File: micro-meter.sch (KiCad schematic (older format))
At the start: 110 parts, among them U1 XC6206P332MR, U2 STM32F411CEU6

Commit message: Fix testpoints
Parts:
- removed TP?: TP_3V3, symbol Connector:TestPoint_2Pole
- removed TP?: TP_I2S, symbol Connector:TestPoint_2Pole
- removed TP?: TP_AIN1, symbol Connector:TestPoint_2Pole
- added R?: 390, symbol Device:R
- added TP?: TP_AIN1, symbol Connector:TestPoint
- added TP? (x3): TP_GND, symbol Connector:TestPoint
- added TP?: TP_DIN, symbol Connector:TestPoint
- added TP?: TP_3V3, symbol Connector:TestPoint
- TP?: symbol Connector:TestPoint_2Pole -> Connector:TestPoint
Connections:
- net +3V3: now also TP?.1
- net AIN1: now also TP?.1
- net GND: now also TP?.1, TP?.1, TP?.1; no longer TP?.2
- net USART1_TX: now also R?.2; no longer U2.30 (PA9)
- net at D?.4 (DIN), R?.1: now also TP?.1
- new net: R?.1, U2.30 (PA9)
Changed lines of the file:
@@
 Comment4 ""
 $EndDescr
-Text GLabel 2300 3250 2    50   Output ~ 0
+Text GLabel 2600 3250 2    50   Output ~ 0
 USART1_TX
 Text GLabel 2300 3350 2    50   Input ~ 0
@@
 	9400 1400 9500 1400
 $Comp
-L Connector:TestPoint_2Pole TP?
+L Connector:TestPoint TP?
 U 1 1 5FAA848A
-P 6850 1800
-F 0 "TP?" V 6800 1650 50  0000 C CNN
-F 1 "TP_AIN0" V 6900 1600 50  0000 C CNN
-F 2 "" H 6850 1800 50  0001 C CNN
-F 3 "~" H 6850 1800 50  0001 C CNN
-	1    6850 1800
-	0    -1   1    0
-$EndComp
-$Comp
-L power:GND #PWR?
-U 1 1 5FAAECA1
-P 6850 2000
-F 0 "#PWR?" H 6850 1750 50  0001 C CNN
-F 1 "GND" H 6855 1827 50  0000 C CNN
-F 2 "" H 6850 2000 50  0001 C CNN
-F 3 "" H 6850 2000 50  0001 C CNN
-	1    6850 2000
-	1    0    0    -1
+P 6850 1600
+F 0 "TP?" H 7000 1750 50  0000 C CNN
+F 1 "TP_AIN0" H 7050 1850 50  0000 C CNN
+F 2 "" H 6850 1600 50  0001 C CNN
+F 3 "~" H 6850 1600 50  0001 C CNN
+	1    6850 1600
+	1    0    0    1
 $EndComp
 $Comp
@@
 Text GLabel 1000 3250 0    50   Output ~ 0
 I2S5_SD
-$Comp
-L Connector:TestPoint_2Pole TP?
-U 1 1 5FAE18DF
-P 3350 5050
-F 0 "TP?" V 3300 5250 50  0000 R CNN
-F 1 "TP_I2S" V 3400 5350 50  0000 R CNN
-F 2 "" H 3350 5050 50  0001 C CNN
-F 3 "~" H 3350 5050 50  0001 C CNN
-	1    3350 5050
-	0    -1   1    0
-$EndComp
 Wire Wire Line
 	3350 4850 3350 4800
@@
 $Comp
 L power:GND #PWR?
-U 1 1 5FAF4159
-P 3350 5250
-F 0 "#PWR?" H 3350 5000 50  0001 C CNN
-F 1 "GND" H 3350 5100 50  0000 C CNN
-F 2 "" H 3350 5250 50  0001 C CNN
-F 3 "" H 3350 5250 50  0001 C CNN
-	1    3350 5250
-	1    0    0    -1
-$EndComp
-$Comp
-L power:GND #PWR?
 U 1 1 5FAF706A
 P 7600 1850
@@
 I2C1_SDA
 $Comp
-L Connector:TestPoint_2Pole TP?
-U 1 1 5FA16E4B
-P 3650 7150
-F 0 "TP?" V 3550 7050 50  0000 R CNN
-F 1 "TP_3V3" V 3650 7100 50  0000 R CNN
-F 2 "" H 3650 7150 50  0001 C CNN
-F 3 "~" H 3650 7150 50  0001 C CNN
-	1    3650 7150
-	0    -1   1    0
-$EndComp
-$Comp
-L power:GND #PWR?
-U 1 1 5FA2498C
-P 3650 7350
-F 0 "#PWR?" H 3650 7100 50  0001 C CNN
-F 1 "GND" H 3655 7177 50  0000 C CNN
-F 2 "" H 3650 7350 50  0001 C CNN
-F 3 "" H 3650 7350 50  0001 C CNN
-	1    3650 7350
-	1    0    0    -1
-$EndComp
-$Comp
 L power:+5V #PWR?
 U 1 1 5FAB374C
@@
 Wire Wire Line
 	3650 6900 3650 6950
-Connection ~ 3650 6950
 Wire Wire Line
 	1300 6600 1400 6600
@@
 	5300 3500 5400 3500
 $Comp
-L Connector:TestPoint_2Pole TP?
-U 1 1 5FB723B7
-P 6850 3400
-F 0 "TP?" V 6800 3250 50  0000 C CNN
-F 1 "TP_AIN1" V 6900 3200 50  0000 C CNN
-F 2 "" H 6850 3400 50  0001 C CNN
-F 3 "~" H 6850 3400 50  0001 C CNN
-	1    6850 3400
-	0    -1   1    0
-$EndComp
-$Comp
-L power:GND #PWR?
-U 1 1 5FB723C1
-P 6850 3600
-F 0 "#PWR?" H 6850 3350 50  0001 C CNN
-F 1 "GND" H 6855 3427 50  0000 C CNN
-F 2 "" H 6850 3600 50  0001 C CNN
-F 3 "" H 6850 3600 50  0001 C CNN
-	1    6850 3600
-	1    0    0    -1
-$EndComp
-$Comp
 L power:GND #PWR?
 U 1 1 5FB723CB
@@
 NoConn ~ 1000 2150
 NoConn ~ 1000 2250
+$Comp
+L Device:R R?
+U 1 1 5FA72209
+P 2450 3250
+F 0 "R?" V 2550 3250 50  0000 C CNN
+F 1 "390" V 2450 3250 50  0000 C CNN
+F 2 "" V 2380 3250 50  0001 C CNN
+F 3 "~" H 2450 3250 50  0001 C CNN
+	1    2450 3250
+	0    -1   -1   0
+$EndComp
+$Comp
+L Connector:TestPoint TP?
+U 1 1 5FA74280
+P 6850 3200
+F 0 "TP?" H 7000 3350 50  0000 C CNN
+F 1 "TP_AIN1" H 7050 3450 50  0000 C CNN
+F 2 "" H 6850 3200 50  0001 C CNN
+F 3 "~" H 6850 3200 50  0001 C CNN
+	1    6850 3200
+	1    0    0    1
+$EndComp
+$Comp
+L Connector:TestPoint TP?
+U 1 1 5FA74EF4
+P 7350 2400
+F 0 "TP?" H 7500 2550 50  0000 C CNN
+F 1 "TP_GND" H 7550 2450 50  0000 C CNN
+F 2 "" H 7350 2400 50  0001 C CNN
+F 3 "~" H 7350 2400 50  0001 C CNN
+	1    7350 2400
+	-1   0    0    -1
+$EndComp
+$Comp
+L power:GND #PWR?
+U 1 1 5FA75CB9
+P 7350 2400
+F 0 "#PWR?" H 7350 2150 50  0001 C CNN
+F 1 "GND" H 7355 2227 50  0000 C CNN
+F 2 "" H 7350 2400 50  0001 C CNN
+F 3 "" H 7350 2400 50  0001 C CNN
+	1    7350 2400
+	1    0    0    -1
+$EndComp
+$Comp
+L Connector:TestPoint TP?
+U 1 1 5FA76A9B
+P 3350 4850
+F 0 "TP?" H 3500 4850 50  0000 C CNN
+F 1 "TP_DIN" H 3550 4950 50  0000 C CNN
+F 2 "" H 3350 4850 50  0001 C CNN
+F 3 "~" H 3350 4850 50  0001 C CNN
+	1    3350 4850
+	-1   0    0    1
+$EndComp
+$Comp
+L Connector:TestPoint TP?
+U 1 1 5FA8B826
+P 3350 5250
+F 0 "TP?" H 3500 5350 50  0000 C CNN
+F 1 "TP_GND" H 3550 5250 50  0000 C CNN
+F 2 "" H 3350 5250 50  0001 C CNN
+F 3 "~" H 3350 5250 50  0001 C CNN
+	1    3350 5250
+	-1   0    0    -1
+$EndComp
+$Comp
+L power:GND #PWR?
+U 1 1 5FA8B830
+P 3350 5250
+F 0 "#PWR?" H 3350 5000 50  0001 C CNN
+F 1 "GND" H 3350 5100 50  0000 C CNN
+F 2 "" H 3350 5250 50  0001 C CNN
+F 3 "" H 3350 5250 50  0001 C CNN
+	1    3350 5250
+	1    0    0    -1
+$EndComp
+$Comp
+L Connector:TestPoint TP?
+U 1 1 5FAB9DCD
+P 3650 6950
+F 0 "TP?" H 3800 7000 50  0000 C CNN
+F 1 "TP_3V3" H 3850 7100 50  0000 C CNN
+F 2 "" H 3650 6950 50  0001 C CNN
+F 3 "~" H 3650 6950 50  0001 C CNN
+	1    3650 6950
+	1    0    0    1
+$EndComp
+$Comp
+L Connector:TestPoint TP?
+U 1 1 5FAB9DD7
+P 3650 7350
+F 0 "TP?" H 3800 7450 50  0000 C CNN
+F 1 "TP_GND" H 3850 7350 50  0000 C CNN
+F 2 "" H 3650 7350 50  0001 C CNN
+F 3 "~" H 3650 7350 50  0001 C CNN
+	1    3650 7350
+	1    0    0    -1
+$EndComp
+$Comp
+L power:GND #PWR?
+U 1 1 5FAB9DE1
+P 3650 7350
+F 0 "#PWR?" H 3650 7100 50  0001 C CNN
+F 1 "GND" H 3650 7200 50  0000 C CNN
+F 2 "" H 3650 7350 50  0001 C CNN
+F 3 "" H 3650 7350 50  0001 C CNN
+	1    3650 7350
+	1    0    0    -1
+$EndComp
+Connection ~ 3650 6950
 $EndSCHEMATC

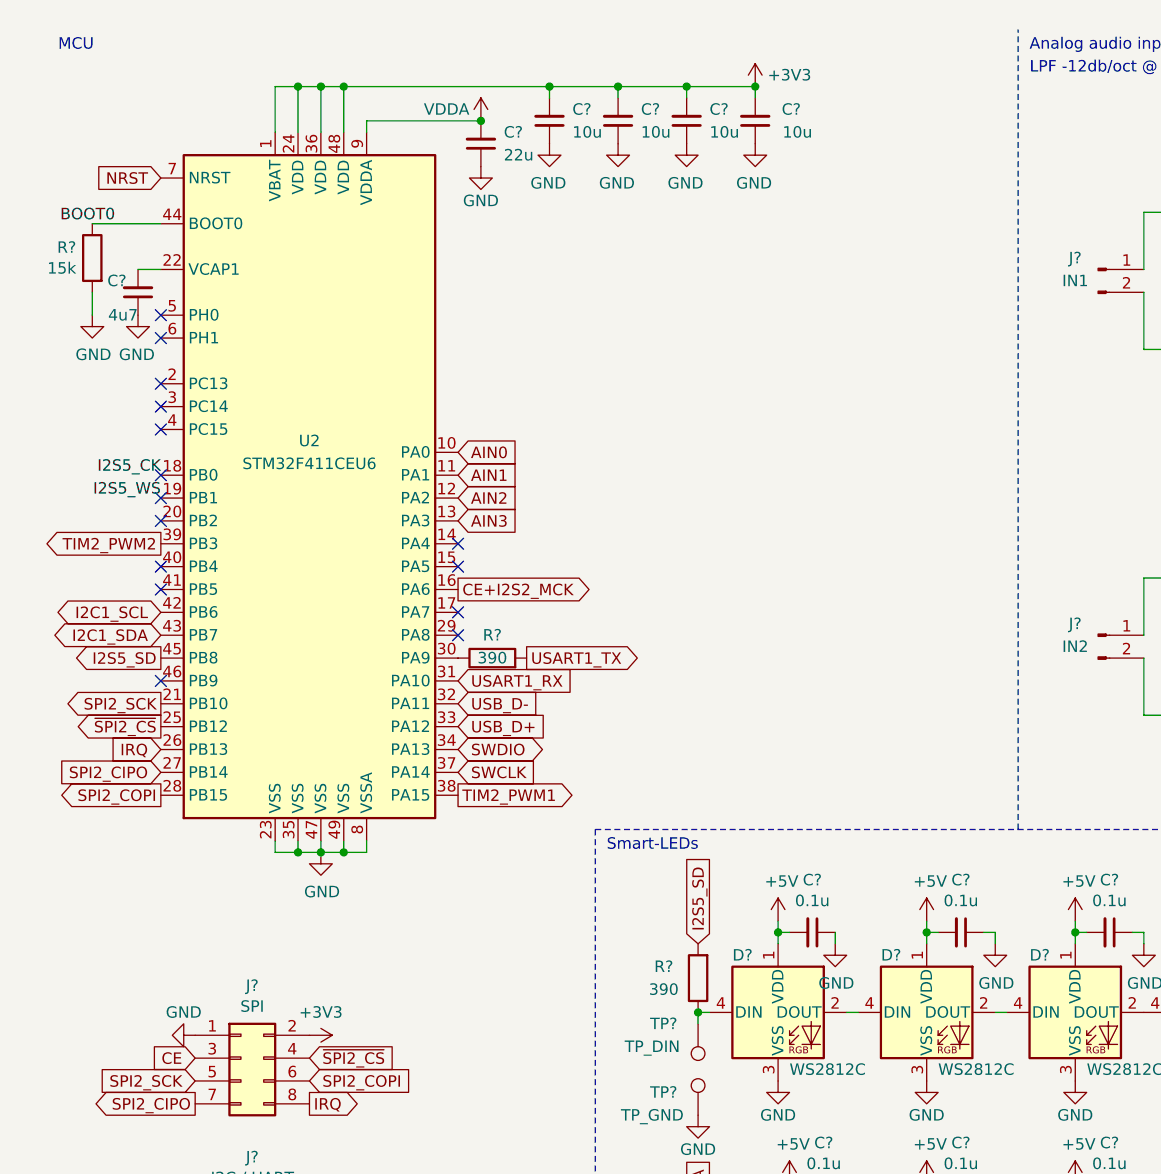
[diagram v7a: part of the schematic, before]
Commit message: Add series terminations
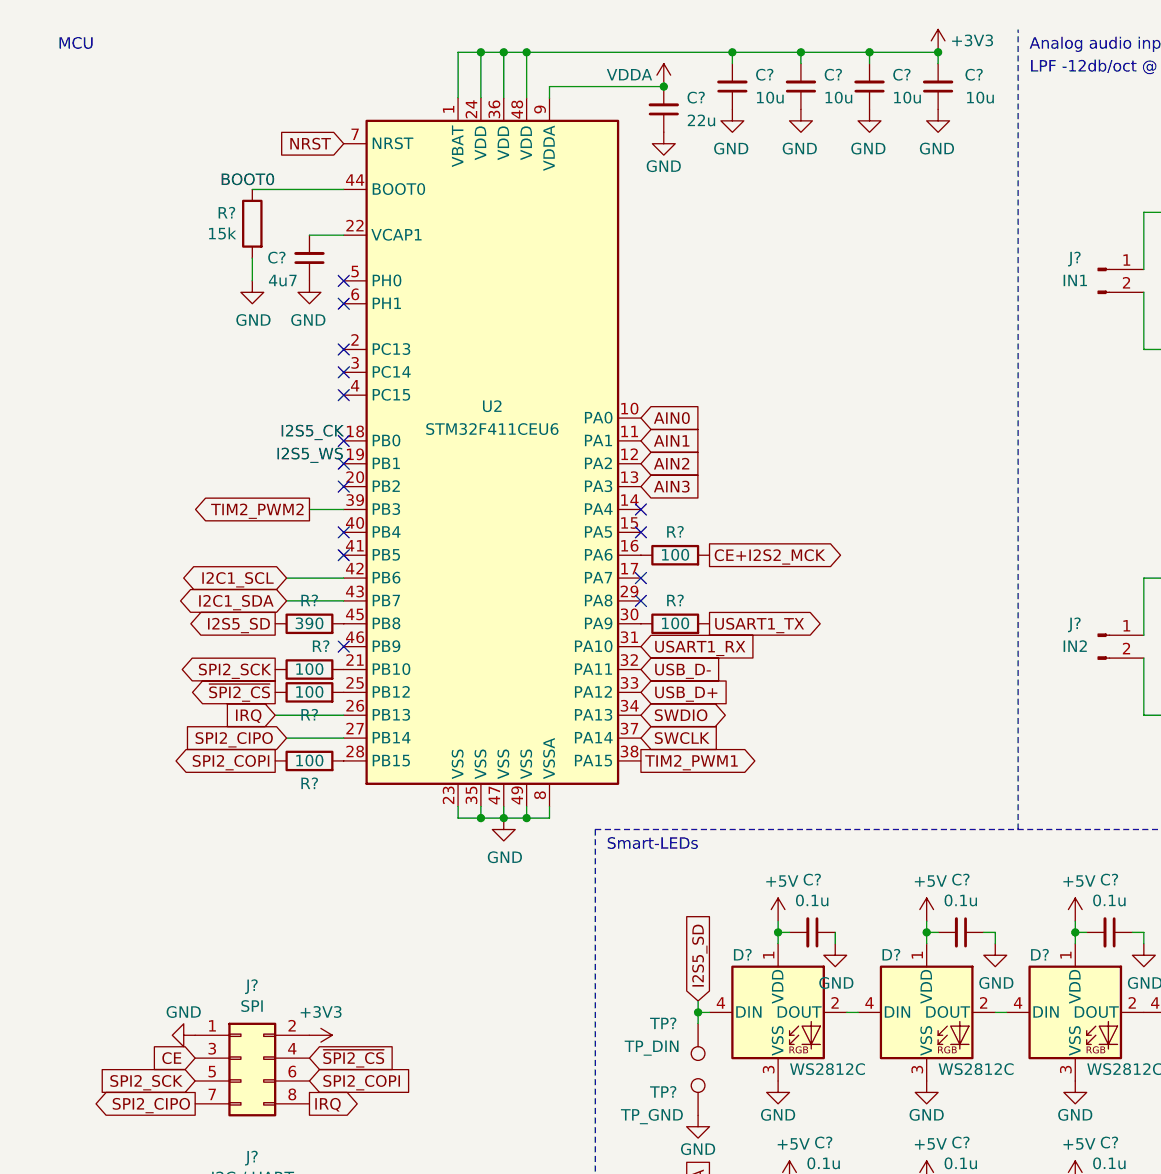
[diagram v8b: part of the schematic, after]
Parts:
- removed R? (x2): 390, symbol Device:R
- added R? (x5): 100, symbol Device:R
- added R?: 390, symbol Device:R
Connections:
- net CE+I2S2_MCK: now also R?.2; no longer U2.16 (PA6)
- net I2S5_SD: now also D?.4 (DIN), TP?.1, R?.1; no longer U2.45 (PB8)
- net SPI2_COPI: now also R?.1; no longer U2.28 (PB15)
- net SPI2_SCK: now also R?.1; no longer U2.21 (PB10)
- net USART1_TX: now also R?.2
- net ~SPI2_CS: now also R?.1; no longer U2.25 (PB12)
- net at U2.30 (PA9): now also R?.1
- new net: R?.2, U2.21 (PB10)
- new net: R?.2, U2.25 (PB12)
- new net: R?.2, U2.28 (PB15)
- new net: R?.2, U2.45 (PB8)
- new net: R?.1, U2.16 (PA6)
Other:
- moved on the sheet: C?, R?, U2
